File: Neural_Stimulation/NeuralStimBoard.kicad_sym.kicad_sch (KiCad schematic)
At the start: 61 parts, among them U1 CSI040

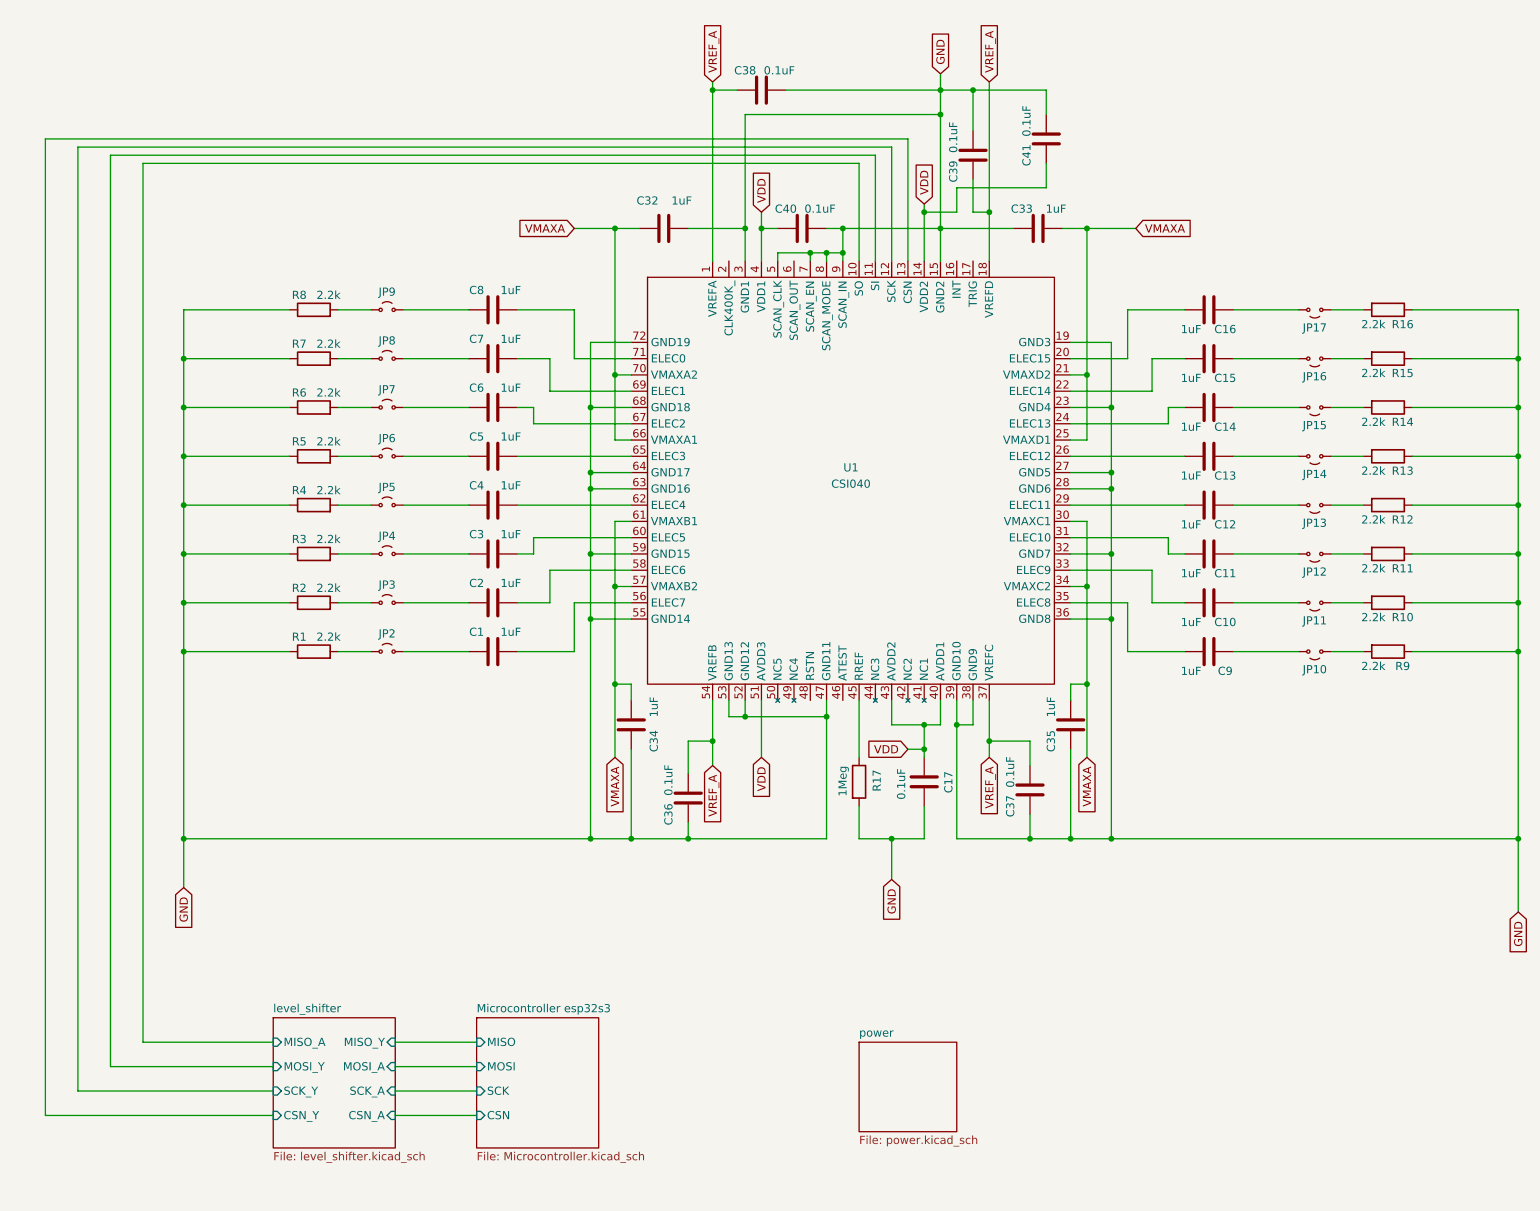
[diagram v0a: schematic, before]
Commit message: Added INT, TRIG, ATEST and RSTN pin circuits
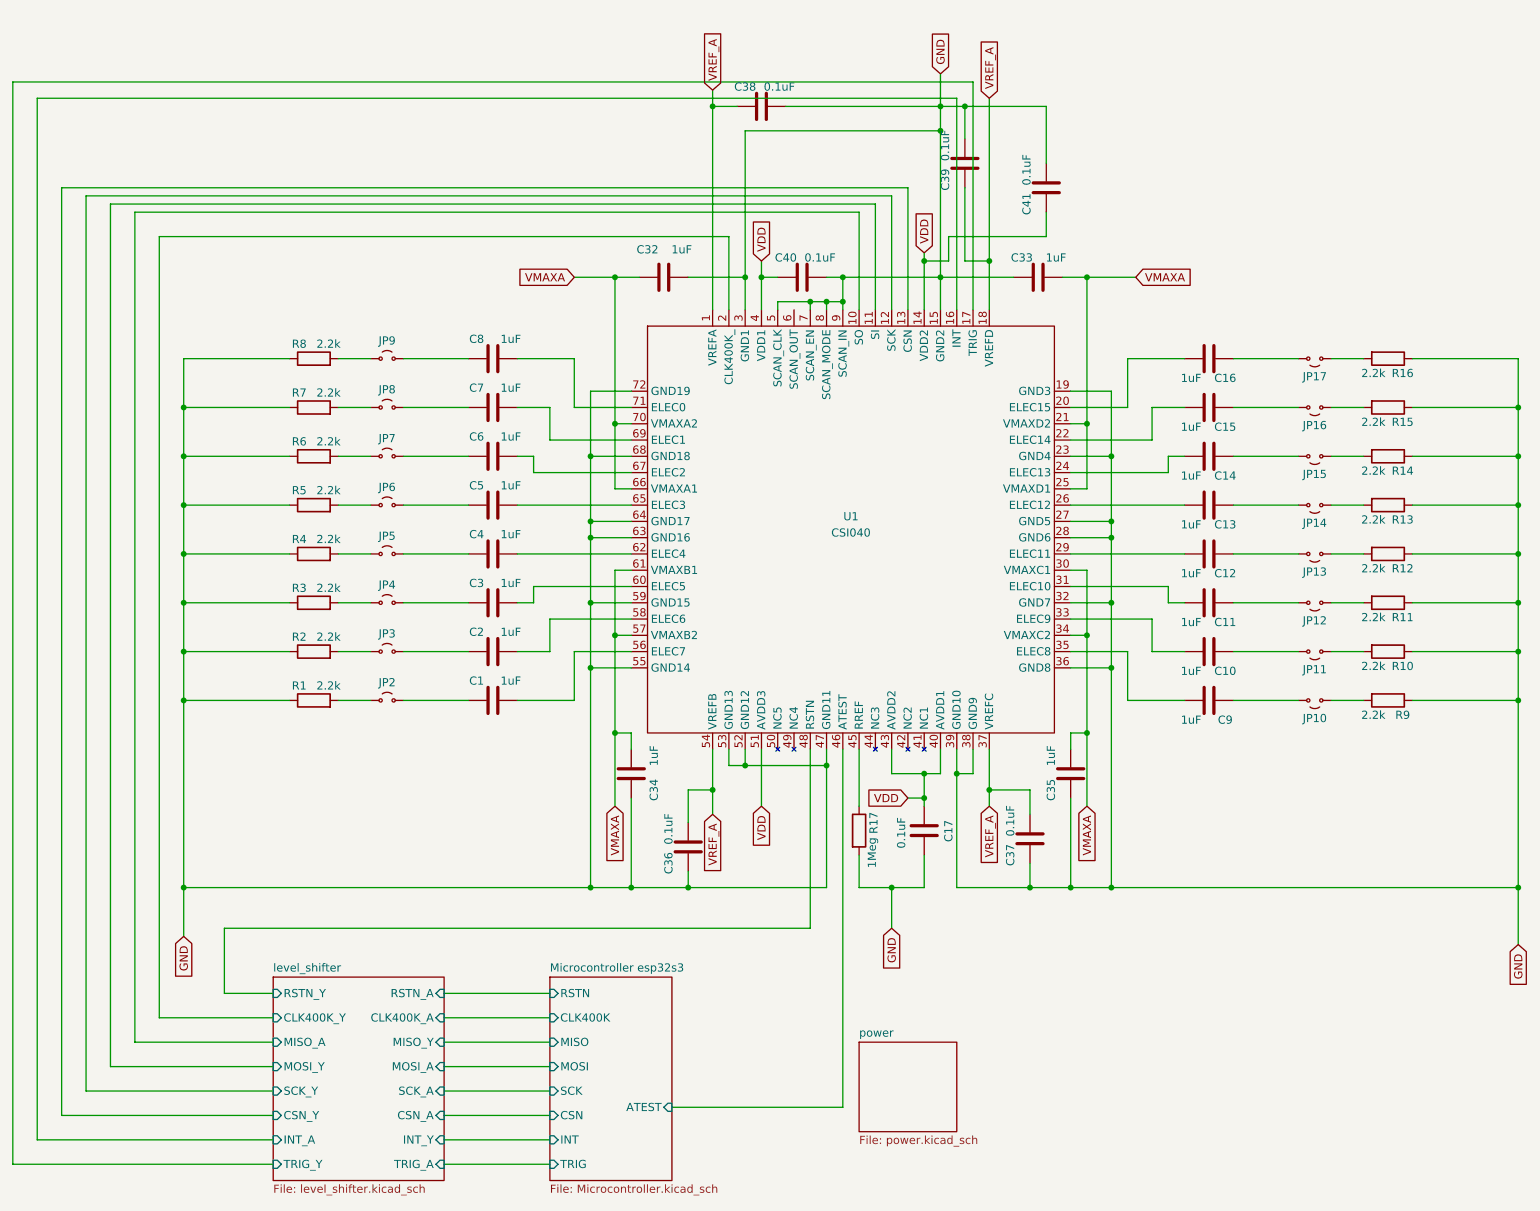
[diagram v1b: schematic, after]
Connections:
- net level_shifter/INT_A: now reaches U1.16 (INT)
- net level_shifter/TRIG_Y: now reaches U1.17 (TRIG)
- net level_shifter/CLK400K_Y: now reaches U1.2 (CLK400K_)
- net Microcontroller esp32s3/ATEST: now reaches U1.46 (ATEST)
- net level_shifter/RSTN_Y: now reaches U1.48 (RSTN)
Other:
- sheet Microcontroller esp32s3 ports: added ATEST, CLK400K, INT, RSTN, TRIG; removed none
- sheet level_shifter ports: added CLK400K_A, CLK400K_Y, INT_A, INT_Y, RSTN_A, RSTN_Y, TRIG_A, TRIG_Y; removed none
- moved on the sheet: C1, C10, C11, C12, C13, C14, C15, C16, C17, C2, C3, C32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
